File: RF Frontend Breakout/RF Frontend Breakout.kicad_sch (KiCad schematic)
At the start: 57 parts, among them IC1 QPC1022SR, IC2 GRF5504, IC3 LHA-13LN+, IC4 QPC1022SR, J1 Conn_Coaxial, J2 Conn_Coaxial, J3 Conn_Coaxial, U1 NCS-62+

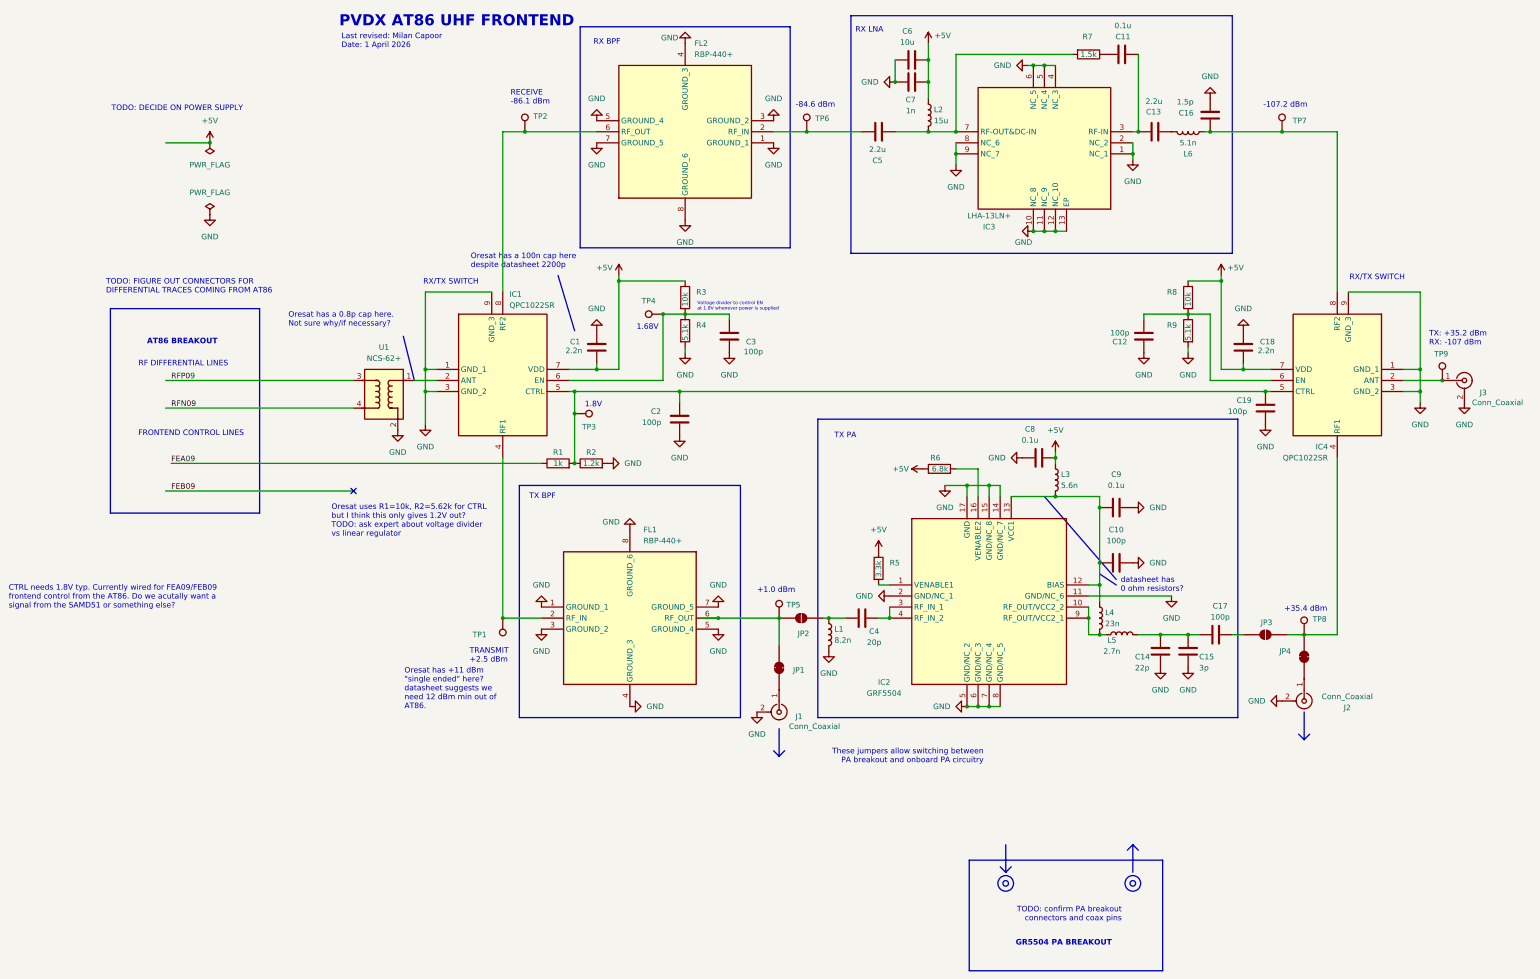
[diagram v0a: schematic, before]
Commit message: initial frontend layout
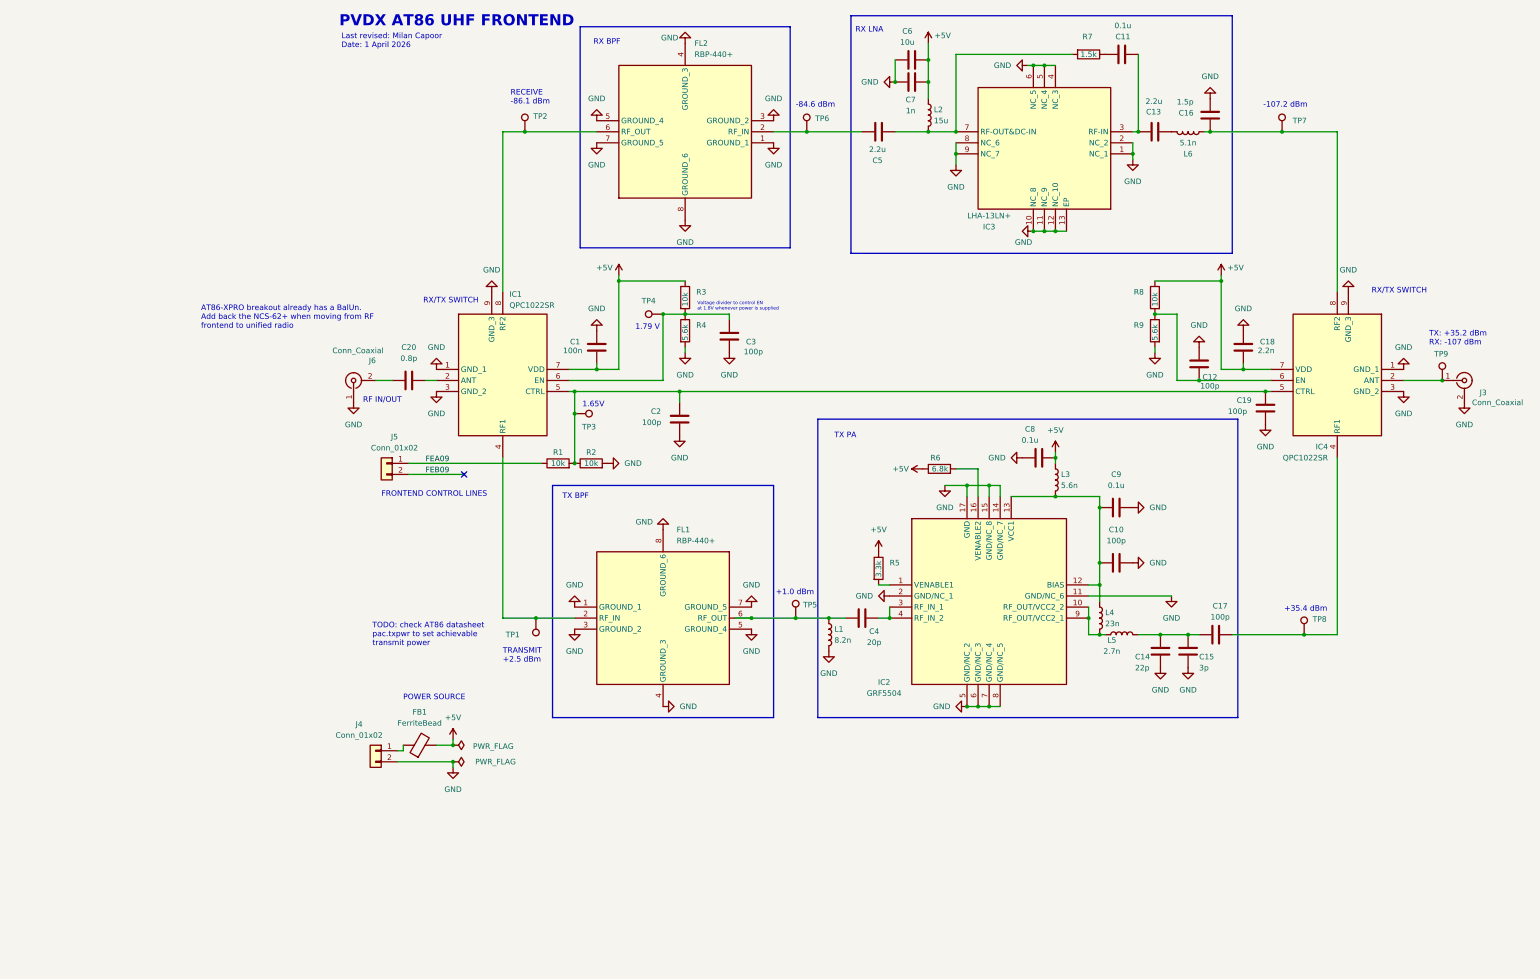
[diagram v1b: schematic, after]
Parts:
- removed J1, J2: Conn_Coaxial, symbol Connector:Conn_Coaxial
- removed JP1, JP4: SolderJumper_2_Bridged, Jumper:SolderJumper-2_P1.3mm_Bridged2Bar_RoundedPad1.0x1.5mm, symbol Jumper:SolderJumper_2_Bridged
- removed JP2, JP3: SolderJumper_2_Open, Jumper:SolderJumper-2_P1.3mm_Open_RoundedPad1.0x1.5mm, symbol Jumper:SolderJumper_2_Open
- removed U1: NCS-62+, RF Frontend Footprints:NCS262, symbol NCS2-62+:NCS2-62+_Custom
- added C20: 0.8p, Capacitor_SMD:C_0603_1608Metric, symbol Device:C
- added FB1: FerriteBead, symbol Device:FerriteBead
- added J4, J5: Conn_01x02, Connector_PinSocket_2.54mm:PinSocket_1x02_P2.54mm_Vertical, symbol Connector_Generic:Conn_01x02
- added J6: Conn_Coaxial, Connector_Coaxial:SMA_Molex_73251-1153_EdgeMount_Horizontal, symbol Connector:Conn_Coaxial
- C1: value 2.2n -> 100n; footprint Capacitor_SMD:C_0402_1005Metric -> Capacitor_SMD:C_0603_1608Metric
- C10, C11, C12, C13, C14, C15, C16, C17, C18, C19, C2, C3, C4, C7, C8, C9: footprint Capacitor_SMD:C_0402_1005Metric -> Capacitor_SMD:C_0603_1608Metric
- J3: footprint (none) -> Connector_Coaxial:SMA_Molex_73251-1153_EdgeMount_Horizontal
- L1: footprint Inductor_SMD:L_0402_1005Metric -> Inductor_SMD:L_0603_1608Metric
- L3: footprint Inductor_SMD:L_0402_1005Metric -> Inductor_SMD:L_0805_2012Metric
- R1: value 1k -> 10k; footprint Resistor_SMD:R_0402_1005Metric -> Resistor_SMD:R_0603_1608Metric
- R2: value 1.2k -> 10k; footprint Resistor_SMD:R_0402_1005Metric -> Resistor_SMD:R_0603_1608Metric
- R3, R5, R6, R7, R8: footprint Resistor_SMD:R_0402_1005Metric -> Resistor_SMD:R_0603_1608Metric
- R4, R9: value 5.1k -> 5.6k; footprint Resistor_SMD:R_0402_1005Metric -> Resistor_SMD:R_0603_1608Metric
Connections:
- net +5V: now also FB1.2
- net FEA09: now also J5.1 (Pin_1)
- net FEB09: now also J5.2 (Pin_2)
- net GND: now also J4.2 (Pin_2), J6.1 (In)
- net at C17.2: now also IC4.4 (RF1), TP8.1
- net at FL1.6 (RF_OUT), TP5.1: now also C4.1, L1.1
- net at IC1.2 (ANT): now also C20.2
- new net: FB1.1, J4.1 (Pin_1)
- new net: C20.1, J6.2 (Ext)
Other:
- note added: "1.65V"
- note added: "1.79 V"
- note added: "AT86-XPRO breakout already has a BalUn. Add back the NCS-62+ when moving from RF frontend to unified radio"
- note added: "POWER SOURCE"
- note added: "RF IN/OUT"
- note added: "TODO: check AT86 datasheet pac.txpwr to set achievable transmit power"
- note removed: "1.68V"
- note removed: "1.8V"
- note removed: "AT86 BREAKOUT"
- note removed: "CTRL needs 1.8V typ. Currently wired for FEA09/FEB09 frontend control from the AT86. Do we acutally want a signal from the SAMD51 or something else?"
- note removed: "GR5504 PA BREAKOUT"
- note removed: "Oresat has +11 dBm "single ended" here? datasheet suggests we need 12 dBm min out of AT86."
- note removed: "Oresat has a 0.8p cap here. Not sure why/if necessary?"
- note removed: "Oresat has a 100n cap here despite datasheet 2200p"
- note removed: "Oresat uses R1=10k, R2=5.62k for CTRL but I think this only gives 1.2V out? TODO: ask expert about voltage divider vs linear regulator"
- note removed: "RF DIFFERENTIAL LINES"
- note removed: "TODO: DECIDE ON POWER SUPPLY"
- note removed: "TODO: FIGURE OUT CONNECTORS FOR DIFFERENTIAL TRACES COMING FROM AT86"
- note removed: "TODO: confirm PA breakout connectors and coax pins"
- note removed: "These jumpers allow switching between PA breakout and onboard PA circuitry"
- note removed: "datasheet has 0 ohm resistors?"
- moved on the sheet: C12, FL1, R8, R9, TP1, TP5

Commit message: test
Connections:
- net GND: now also J6.2 (Ext); no longer J6.1 (In)
- net at C20.1: now also J6.1 (In); no longer J6.2 (Ext)
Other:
- moved on the sheet: J6
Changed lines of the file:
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@@
 	(symbol
 		(lib_id "power:GND")
-		(at 19.05 106.68 0)
+		(at 19.05 96.52 180)
 		(unit 1)
 		(body_style 1)
@@
 		(fields_autoplaced yes)
 		(property "Reference" "#PWR021"
-			(at 19.05 113.03 0)
+			(at 19.05 90.17 0)
 			(hide yes)
 			(show_name no)
@@
 		)
 		(property "Value" "GND"
-			(at 19.05 111.76 0)
-			(show_name no)
-			(do_not_autoplace no)
-			(effects
-				(font
-					(size 1.27 1.27)
-				)
+			(at 21.59 95.2499 0)
+			(show_name no)
+			(do_not_autoplace no)
+			(effects
+				(font
+					(size 1.27 1.27)
+				)
+				(justify right)
 			)
 		)
 		(property "Footprint" ""
-			(at 19.05 106.68 0)
-			(hide yes)
-			(show_name no)
-			(do_not_autoplace no)
-			(effects
-				(font
-					(size 1.27 1.27)
-				)
-			)
-		)
-		(property "Datasheet" ""
-			(at 19.05 106.68 0)
+			(at 19.05 96.52 0)
+			(hide yes)
+			(show_name no)
+			(do_not_autoplace no)
+			(effects
+				(font
+					(size 1.27 1.27)
+				)
+			)
+		)
+		(property "Datasheet" ""
+			(at 19.05 96.52 0)
 			(hide yes)
 			(show_name no)
@@
 		)
 		(property "Description" "Power symbol creates a global label with name \"GND\" , ground"
-			(at 19.05 106.68 0)
+			(at 19.05 96.52 0)
 			(hide yes)
 			(show_name no)
@@
 	(symbol
 		(lib_id "Connector:Conn_Coaxial")
-		(at 19.05 101.6 90)
+		(at 19.05 101.6 180)
 		(unit 1)
 		(body_style 1)
@@
 		(dnp no)
 		(property "Reference" "J6"
-			(at 23.368 97.028 90)
+			(at 14.478 97.282 90)
 			(show_name no)
 			(do_not_autoplace no)
@@
 		)
 		(property "Value" "Conn_Coaxial"
-			(at 20.066 94.742 90)
-			(show_name no)
-			(do_not_autoplace no)
+			(at 12.192 100.584 90)
+			(show_name no)
+			(do_not_autoplace no)

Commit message: finished pcb
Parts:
- removed FB1: FerriteBead, symbol Device:FerriteBead
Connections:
- net +5V: now also J4.1 (Pin_1)
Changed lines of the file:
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@@
 	)
 	(rectangle
-		(start 133.35 17.78)
-		(end 220.98 72.39)
+		(start 45.72 17.78)
+		(end 133.35 72.39)
 		(stroke
 			(width 0)
@@
 	)
 	(junction
-		(at 41.91 185.42)
+		(at 41.91 186.69)
 		(diameter 0)
 		(color 0 0 0 0)
@@
 	(wire
 		(pts
-			(xy 41.91 184.15) (xy 41.91 185.42)
+			(xy 41.91 185.42) (xy 41.91 186.69)
 		)
 		(stroke
@@
 	(wire
 		(pts
-			(xy 30.48 185.42) (xy 30.48 186.69)
-		)
-		(stroke
-			(width 0)
-			(type default)
-		)
-	)
-	(wire
-		(pts
 			(xy 69.85 104.14) (xy 93.98 104.14)
 		)
@@
 	(wire
 		(pts
-			(xy 38.1 185.42) (xy 41.91 185.42)
-		)
-		(stroke
-			(width 0)
-			(type default)
-		)
-	)
-	(wire
-		(pts
 			(xy 245.11 119.38) (xy 245.11 160.02)
 		)
@@
 	(wire
 		(pts
-			(xy 30.48 186.69) (xy 29.21 186.69)
+			(xy 29.21 186.69) (xy 41.91 186.69)
 		)
 		(stroke
@@
 	)
 	(symbol
-		(lib_id "Device:FerriteBead")
-		(at 34.29 185.42 90)
-		(unit 1)
-		(body_style 1)
-		(exclude_from_sim no)
-		(in_bom yes)
-		(on_board yes)
-		(in_pos_files yes)
-		(dnp no)
-		(fields_autoplaced yes)
-		(property "Reference" "FB1"
-			(at 34.2392 177.8 90)
-			(show_name no)
-			(do_not_autoplace no)
-			(effects
-				(font
-					(size 1.27 1.27)
-				)
-			)
-		)
-		(property "Value" "FerriteBead"
-			(at 34.2392 180.34 90)
-			(show_name no)
-			(do_not_autoplace no)
-			(effects
-				(font
-					(size 1.27 1.27)
-				)
-			)
-		)
-		(property "Footprint" ""
-			(at 34.29 187.198 90)
-			(hide yes)
-			(show_name no)
-			(do_not_autoplace no)
-			(effects
-				(font
-					(size 1.27 1.27)
-				)
-			)
-		)
-		(property "Datasheet" ""
-			(at 34.29 185.42 0)
-			(hide yes)
-			(show_name no)
-			(do_not_autoplace no)
-			(effects
-				(font
-					(size 1.27 1.27)
-				)
-			)
-		)
-		(property "Description" "Ferrite bead"
-			(at 34.29 185.42 0)
-			(hide yes)
-			(show_name no)
-			(do_not_autoplace no)
-			(effects
-				(font
-					(size 1.27 1.27)
-				)
-			)
-		)
-		(pin "1"
-		)
-		(pin "2"
-		)
-		(instances
-			(project "RF Frontend Breakout"
-				(path "/1be17eac-b555-466e-8bd3-43262e2e1b9c"
-					(reference "FB1")
-					(unit 1)
-				)
-			)
-		)
-	)
-	(symbol
 		(lib_id "power:GND")
 		(at 90.17 135.89 180)
@@
 	(symbol
 		(lib_id "power:PWR_FLAG")
-		(at 41.91 185.42 270)
+		(at 41.91 186.69 270)
 		(unit 1)
 		(body_style 1)
@@
 		(dnp no)
 		(property "Reference" "#FLG01"
-			(at 43.815 185.42 0)
+			(at 43.815 186.69 0)
 			(hide yes)
 			(show_name no)
@@
 		)
 		(property "Value" "PWR_FLAG"
-			(at 46.482 185.674 90)
+			(at 46.482 186.944 90)
 			(show_name no)
 			(do_not_autoplace no)
@@
 		)
 		(property "Footprint" ""
-			(at 41.91 185.42 0)
+			(at 41.91 186.69 0)
 			(hide yes)
 			(show_name no)
@@
 		)
 		(property "Datasheet" ""
-			(at 41.91 185.42 0)
+			(at 41.91 186.69 0)
 			(hide yes)
 			(show_name no)
@@
 		)
 		(property "Description" "Special symbol for telling ERC where power comes from"
-			(at 41.91 185.42 0)
+			(at 41.91 186.69 0)
 			(hide yes)
 			(show_name no)
@@
 		(in_pos_files yes)
 		(dnp no)
-		(fields_autoplaced yes)
 		(property "Reference" "#PWR025"
 			(at 139.7 144.78 0)
@@
 	(symbol
 		(lib_id "power:+5V")
-		(at 41.91 184.15 0)
+		(at 41.91 185.42 0)
 		(unit 1)
 		(body_style 1)
@@
 		(fields_autoplaced yes)
 		(property "Reference" "#PWR01"
-			(at 41.91 187.96 0)
+			(at 41.91 189.23 0)
 			(hide yes)
 			(show_name no)
@@
 		)
 		(property "Value" "+5V"
-			(at 41.91 179.07 0)
+			(at 41.91 180.34 0)
 			(show_name no)
 			(do_not_autoplace no)
@@
 		)
 		(property "Footprint" ""
-			(at 41.91 184.15 0)
+			(at 41.91 185.42 0)
 			(hide yes)
 			(show_name no)
@@
 		)
 		(property "Datasheet" ""
-			(at 41.91 184.15 0)
+			(at 41.91 185.42 0)
 			(hide yes)
 			(show_name no)
@@
 		)
 		(property "Description" "Power symbol creates a global label with name \"+5V\""
-			(at 41.91 184.15 0)
+			(at 41.91 185.42 0)
 			(hide yes)
 			(show_name no)
